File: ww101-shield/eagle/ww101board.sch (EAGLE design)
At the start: 57 parts

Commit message: Updated Test Program
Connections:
- net MB0: now also JP1.2, R10.2, U$7.P0[1]; no longer JP1.1, R9.2, U$7.P0[0]
- net MB1: now also JP1.1, R9.2, U$7.P0[0]; no longer JP1.2, R10.2, U$7.P0[1]
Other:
- moved on the sheet: MB0, MB1, R10, R9
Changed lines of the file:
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@@
 <?xml version="1.0" encoding="utf-8"?>
 <!DOCTYPE eagle SYSTEM "eagle.dtd">
-<eagle version="7.7.0">
+<eagle version="7.6.0">
 <drawing>
 <settings>
@@
 <parts>
 <part name="U$2" library="IOTExpert" deviceset="U8G-096-OLED" device=""/>
+<part name="MB1" library="IOTExpert" deviceset="EVQPE1" device=""/>
 <part name="MB0" library="IOTExpert" deviceset="EVQPE1" device=""/>
-<part name="MB1" library="IOTExpert" deviceset="EVQPE1" device=""/>
 <part name="U$7" library="PatternAgents-Cypress" deviceset="CY8C4A45-48" device=""/>
 <part name="C1" library="PatternAgents-ProtoPads" deviceset="CAP" device="0603-CAP" value="1uF"/>
@@
 <instances>
 <instance part="U$2" gate="G$1" x="114.3" y="53.34"/>
-<instance part="MB0" gate="G$1" x="121.92" y="88.9"/>
-<instance part="MB1" gate="G$1" x="121.92" y="76.2"/>
+<instance part="MB1" gate="G$1" x="124.46" y="78.74"/>
+<instance part="MB0" gate="G$1" x="124.46" y="88.9"/>
 <instance part="R2" gate="1" x="149.86" y="53.34"/>
 <instance part="MBLED0" gate="G$1" x="187.96" y="88.9" rot="R90"/>
@@
 <instance part="R7" gate="R" x="198.12" y="88.9" rot="R180"/>
 <instance part="R8" gate="R" x="198.12" y="76.2" rot="R180"/>
-<instance part="R9" gate="R" x="152.4" y="88.9" rot="R180"/>
-<instance part="R10" gate="R" x="152.4" y="76.2" rot="R180"/>
+<instance part="R9" gate="R" x="154.94" y="78.74" rot="R180"/>
+<instance part="R10" gate="R" x="154.94" y="88.9" rot="R180"/>
 <instance part="R30" gate="G$1" x="55.88" y="76.2" rot="MR270"/>
 <instance part="R31" gate="JMP" x="66.04" y="76.2" rot="MR270"/>
@@
 <segment>
 <pinref part="R10" gate="R" pin="1"/>
-<wire x1="157.48" y1="76.2" x2="165.1" y2="76.2" width="0.1524" layer="91"/>
-<wire x1="165.1" y1="76.2" x2="165.1" y2="88.9" width="0.1524" layer="91"/>
+<wire x1="160.02" y1="88.9" x2="167.64" y2="88.9" width="0.1524" layer="91"/>
+<wire x1="167.64" y1="88.9" x2="167.64" y2="78.74" width="0.1524" layer="91"/>
 <pinref part="R9" gate="R" pin="1"/>
-<wire x1="165.1" y1="88.9" x2="157.48" y2="88.9" width="0.1524" layer="91"/>
-<label x="160.02" y="88.9" size="1.778" layer="95"/>
+<wire x1="167.64" y1="78.74" x2="160.02" y2="78.74" width="0.1524" layer="91"/>
+<label x="162.56" y="78.74" size="1.778" layer="95"/>
 </segment>
 <segment>
@@
 </segment>
 </net>
-<net name="MB0" class="0">
-<segment>
-<pinref part="MB0" gate="G$1" pin="P$2"/>
+<net name="MB1" class="0">
+<segment>
+<pinref part="MB1" gate="G$1" pin="P$2"/>
 <pinref part="R9" gate="R" pin="2"/>
-<wire x1="147.32" y1="88.9" x2="132.08" y2="88.9" width="0.1524" layer="91"/>
-<label x="137.16" y="88.9" size="1.778" layer="95"/>
+<wire x1="149.86" y1="78.74" x2="134.62" y2="78.74" width="0.1524" layer="91"/>
+<label x="139.7" y="78.74" size="1.778" layer="95"/>
 </segment>
 </net>
 <net name="GND" class="0">
 <segment>
+<pinref part="MB1" gate="G$1" pin="P$1"/>
+<wire x1="124.46" y1="78.74" x2="119.38" y2="78.74" width="0.1524" layer="91"/>
+<wire x1="119.38" y1="78.74" x2="119.38" y2="88.9" width="0.1524" layer="91"/>
 <pinref part="MB0" gate="G$1" pin="P$1"/>
-<wire x1="121.92" y1="88.9" x2="116.84" y2="88.9" width="0.1524" layer="91"/>
-<wire x1="116.84" y1="88.9" x2="116.84" y2="76.2" width="0.1524" layer="91"/>
-<pinref part="MB1" gate="G$1" pin="P$1"/>
-<wire x1="116.84" y1="76.2" x2="121.92" y2="76.2" width="0.1524" layer="91"/>
-<label x="116.84" y="78.74" size="1.778" layer="95" rot="R90"/>
+<wire x1="119.38" y1="88.9" x2="124.46" y2="88.9" width="0.1524" layer="91"/>
+<label x="119.38" y="91.44" size="1.778" layer="95" rot="R90"/>
 </segment>
 <segment>
@@
 </segment>
 </net>
-<net name="MB1" class="0">
-<segment>
-<pinref part="MB1" gate="G$1" pin="P$2"/>
+<net name="MB0" class="0">
+<segment>
+<pinref part="MB0" gate="G$1" pin="P$2"/>
 <pinref part="R10" gate="R" pin="2"/>
-<wire x1="132.08" y1="76.2" x2="147.32" y2="76.2" width="0.1524" layer="91"/>
-<label x="134.62" y="76.2" size="1.778" layer="95"/>
+<wire x1="134.62" y1="88.9" x2="149.86" y2="88.9" width="0.1524" layer="91"/>
+<label x="137.16" y="88.9" size="1.778" layer="95"/>
 </segment>
 </net>
@@
 </segment>
 </net>
-<net name="MB0" class="0">
+<net name="MB1" class="0">
 <segment>
 <pinref part="U$7" gate="G$1" pin="P0[0]"/>
@@
 </segment>
 </net>
-<net name="MB1" class="0">
+<net name="MB0" class="0">
+<segment>
+<pinref part="JP1" gate="G$1" pin="2"/>
+<wire x1="-25.4" y1="109.22" x2="-10.16" y2="109.22" width="0.1524" layer="91"/>
+<label x="-22.86" y="109.22" size="1.778" layer="95"/>
+</segment>
 <segment>
 <pinref part="U$7" gate="G$1" pin="P0[1]"/>
@@
 <label x="76.2" y="60.96" size="1.778" layer="95"/>
 </segment>
-<segment>
-<pinref part="JP1" gate="G$1" pin="2"/>
-<wire x1="-25.4" y1="109.22" x2="-10.16" y2="109.22" width="0.1524" layer="91"/>
-<label x="-22.86" y="109.22" size="1.778" layer="95"/>
-</segment>
-</net>
+</net>

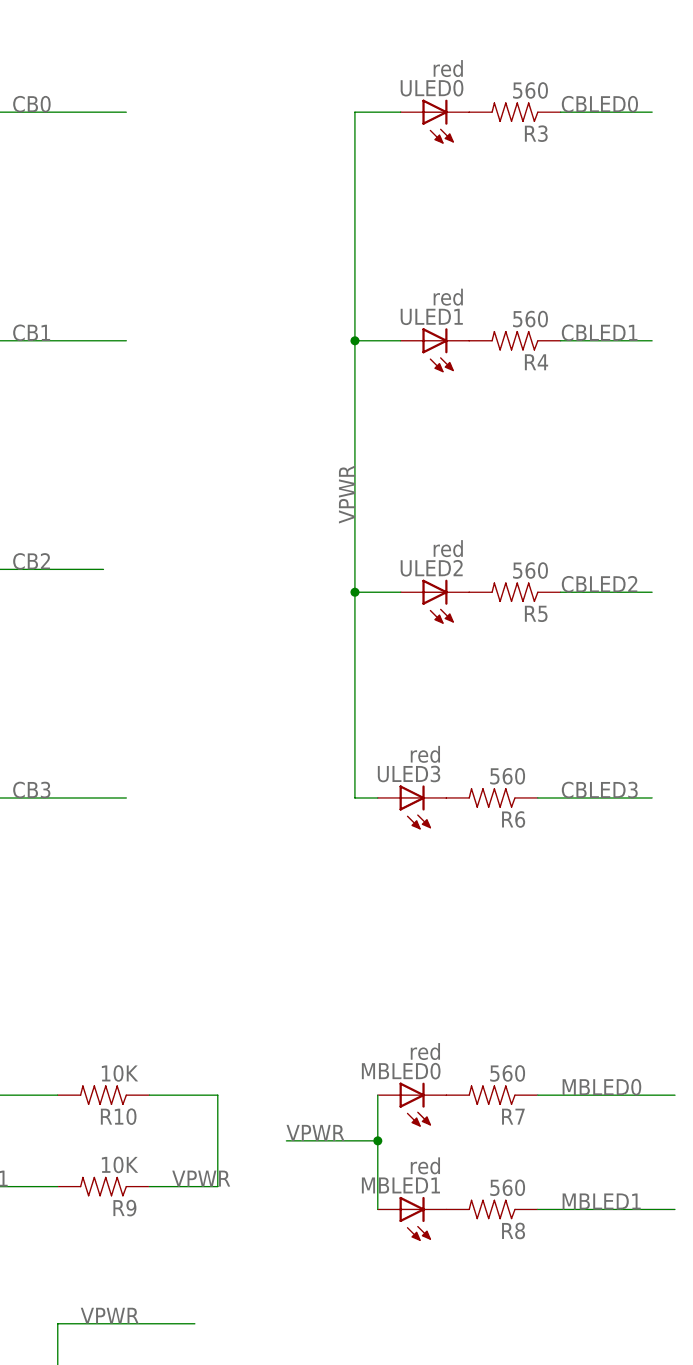
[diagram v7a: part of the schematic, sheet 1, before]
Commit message: Updated silkscreen
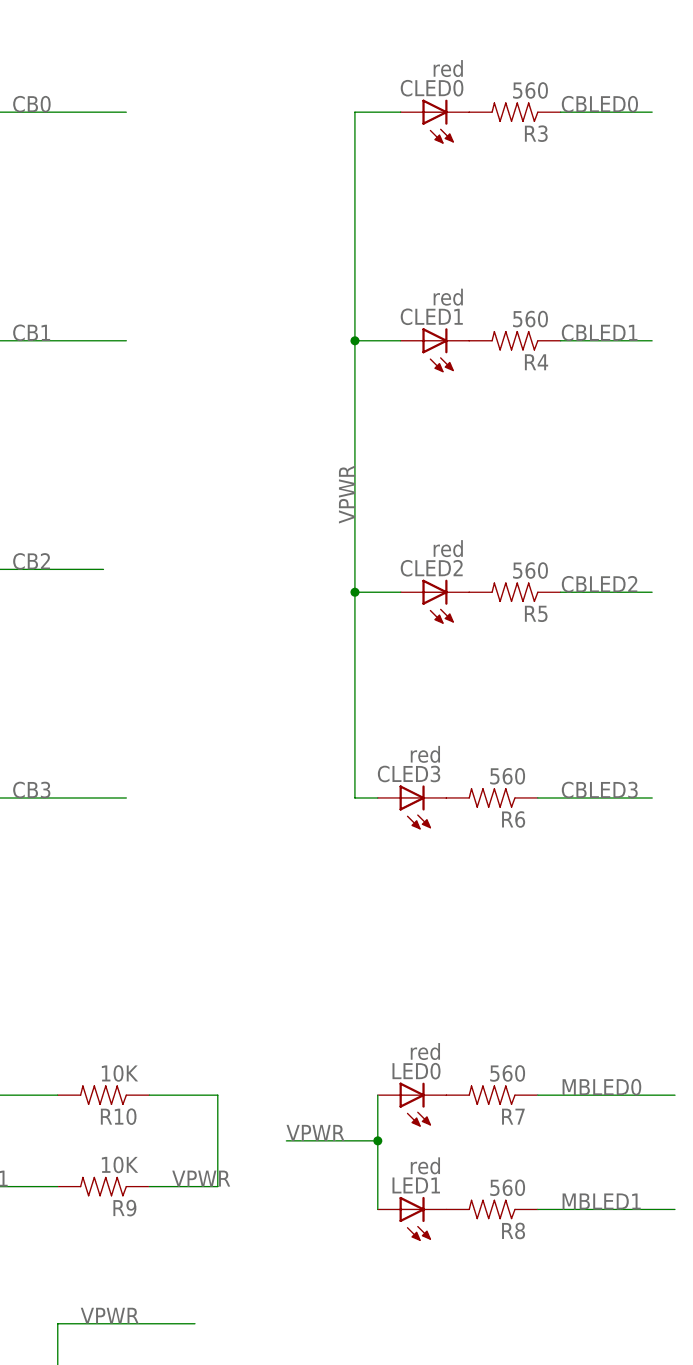
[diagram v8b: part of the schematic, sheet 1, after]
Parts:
- renumbered MBLED0 to LED0, MBLED1 to LED1, ULED0 to CLED0, ULED1 to CLED1, ULED2 to CLED2, ULED3 to CLED3
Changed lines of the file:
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@@
 <?xml version="1.0" encoding="utf-8"?>
 <!DOCTYPE eagle SYSTEM "eagle.dtd">
-<eagle version="7.6.0">
+<eagle version="7.7.0">
 <drawing>
 <settings>
@@
 <part name="C9" library="PatternAgents-ProtoPads" deviceset="CAP" device="0603-CAP" value="0.1uF"/>
 <part name="R2" library="pot" deviceset="TRIM_US-" device="3386P" value="10K"/>
-<part name="MBLED0" library="adafruit" deviceset="LED" device="CHIP-LED0603" value="red"/>
-<part name="MBLED1" library="adafruit" deviceset="LED" device="CHIP-LED0603" value="red"/>
-<part name="ULED0" library="adafruit" deviceset="LED" device="CHIP-LED0603" value="red"/>
-<part name="ULED1" library="adafruit" deviceset="LED" device="CHIP-LED0603" value="red"/>
-<part name="ULED2" library="adafruit" deviceset="LED" device="CHIP-LED0603" value="red"/>
-<part name="ULED3" library="adafruit" deviceset="LED" device="CHIP-LED0603" value="red"/>
+<part name="LED0" library="adafruit" deviceset="LED" device="CHIP-LED0603" value="red"/>
+<part name="LED1" library="adafruit" deviceset="LED" device="CHIP-LED0603" value="red"/>
+<part name="CLED0" library="adafruit" deviceset="LED" device="CHIP-LED0603" value="red"/>
+<part name="CLED1" library="adafruit" deviceset="LED" device="CHIP-LED0603" value="red"/>
+<part name="CLED2" library="adafruit" deviceset="LED" device="CHIP-LED0603" value="red"/>
+<part name="CLED3" library="adafruit" deviceset="LED" device="CHIP-LED0603" value="red"/>
 <part name="R3" library="PatternAgents-ProtoPads" deviceset="RESISTOR" device="0603" value="560"/>
 <part name="R4" library="PatternAgents-ProtoPads" deviceset="RESISTOR" device="0603" value="560"/>
@@
 <instance part="MB0" gate="G$1" x="124.46" y="88.9"/>
 <instance part="R2" gate="1" x="149.86" y="53.34"/>
-<instance part="MBLED0" gate="G$1" x="187.96" y="88.9" rot="R90"/>
-<instance part="MBLED1" gate="G$1" x="187.96" y="76.2" rot="R90"/>
-<instance part="ULED0" gate="G$1" x="190.5" y="198.12" rot="R90"/>
-<instance part="ULED1" gate="G$1" x="190.5" y="172.72" rot="R90"/>
-<instance part="ULED2" gate="G$1" x="190.5" y="144.78" rot="R90"/>
-<instance part="ULED3" gate="G$1" x="187.96" y="121.92" rot="R90"/>
+<instance part="LED0" gate="G$1" x="187.96" y="88.9" rot="R90"/>
+<instance part="LED1" gate="G$1" x="187.96" y="76.2" rot="R90"/>
+<instance part="CLED0" gate="G$1" x="190.5" y="198.12" rot="R90"/>
+<instance part="CLED1" gate="G$1" x="190.5" y="172.72" rot="R90"/>
+<instance part="CLED2" gate="G$1" x="190.5" y="144.78" rot="R90"/>
+<instance part="CLED3" gate="G$1" x="187.96" y="121.92" rot="R90"/>
 <instance part="R3" gate="R" x="200.66" y="198.12" rot="R180"/>
 <instance part="R4" gate="R" x="200.66" y="172.72" rot="R180"/>
@@
 <net name="N$8" class="0">
 <segment>
-<pinref part="ULED0" gate="G$1" pin="C"/>
+<pinref part="CLED0" gate="G$1" pin="C"/>
 <pinref part="R3" gate="R" pin="2"/>
 </segment>
@@
 <net name="N$9" class="0">
 <segment>
-<pinref part="ULED1" gate="G$1" pin="C"/>
+<pinref part="CLED1" gate="G$1" pin="C"/>
 <pinref part="R4" gate="R" pin="2"/>
 </segment>
@@
 <net name="N$10" class="0">
 <segment>
-<pinref part="ULED2" gate="G$1" pin="C"/>
+<pinref part="CLED2" gate="G$1" pin="C"/>
 <pinref part="R5" gate="R" pin="2"/>
 </segment>
@@
 <net name="N$11" class="0">
 <segment>
-<pinref part="ULED3" gate="G$1" pin="C"/>
+<pinref part="CLED3" gate="G$1" pin="C"/>
 <pinref part="R6" gate="R" pin="2"/>
 </segment>
@@
 <net name="VPWR" class="0">
 <segment>
-<pinref part="ULED3" gate="G$1" pin="A"/>
+<pinref part="CLED3" gate="G$1" pin="A"/>
 <wire x1="185.42" y1="121.92" x2="182.88" y2="121.92" width="0.1524" layer="91"/>
 <wire x1="182.88" y1="121.92" x2="182.88" y2="144.78" width="0.1524" layer="91"/>
-<pinref part="ULED0" gate="G$1" pin="A"/>
+<pinref part="CLED0" gate="G$1" pin="A"/>
 <wire x1="182.88" y1="144.78" x2="182.88" y2="172.72" width="0.1524" layer="91"/>
 <wire x1="182.88" y1="172.72" x2="182.88" y2="198.12" width="0.1524" layer="91"/>
 <wire x1="182.88" y1="198.12" x2="187.96" y2="198.12" width="0.1524" layer="91"/>
-<pinref part="ULED1" gate="G$1" pin="A"/>
+<pinref part="CLED1" gate="G$1" pin="A"/>
 <wire x1="187.96" y1="172.72" x2="182.88" y2="172.72" width="0.1524" layer="91"/>
-<pinref part="ULED2" gate="G$1" pin="A"/>
+<pinref part="CLED2" gate="G$1" pin="A"/>
 <wire x1="187.96" y1="144.78" x2="182.88" y2="144.78" width="0.1524" layer="91"/>
 <label x="182.88" y="152.4" size="1.778" layer="95" rot="R90"/>
@@
 <segment>
 <wire x1="185.42" y1="76.2" x2="185.42" y2="83.82" width="0.1524" layer="91"/>
-<pinref part="MBLED0" gate="G$1" pin="A"/>
-<pinref part="MBLED1" gate="G$1" pin="A"/>
+<pinref part="LED0" gate="G$1" pin="A"/>
+<pinref part="LED1" gate="G$1" pin="A"/>
 <wire x1="185.42" y1="83.82" x2="185.42" y2="88.9" width="0.1524" layer="91"/>
 <wire x1="185.42" y1="83.82" x2="175.26" y2="83.82" width="0.1524" layer="91"/>
@@
 <net name="N$12" class="0">
 <segment>
-<pinref part="MBLED0" gate="G$1" pin="C"/>
+<pinref part="LED0" gate="G$1" pin="C"/>
 <pinref part="R7" gate="R" pin="2"/>
 </segment>
@@
 <net name="N$13" class="0">
 <segment>
-<pinref part="MBLED1" gate="G$1" pin="C"/>
+<pinref part="LED1" gate="G$1" pin="C"/>
 <pinref part="R8" gate="R" pin="2"/>
 </segment>
